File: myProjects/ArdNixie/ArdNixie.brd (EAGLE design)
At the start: 100 x 80 mm, 25 parts, among them IC1 74141, IC4 Anode Driver, IC5 SPARKRTC, X5 Seconds

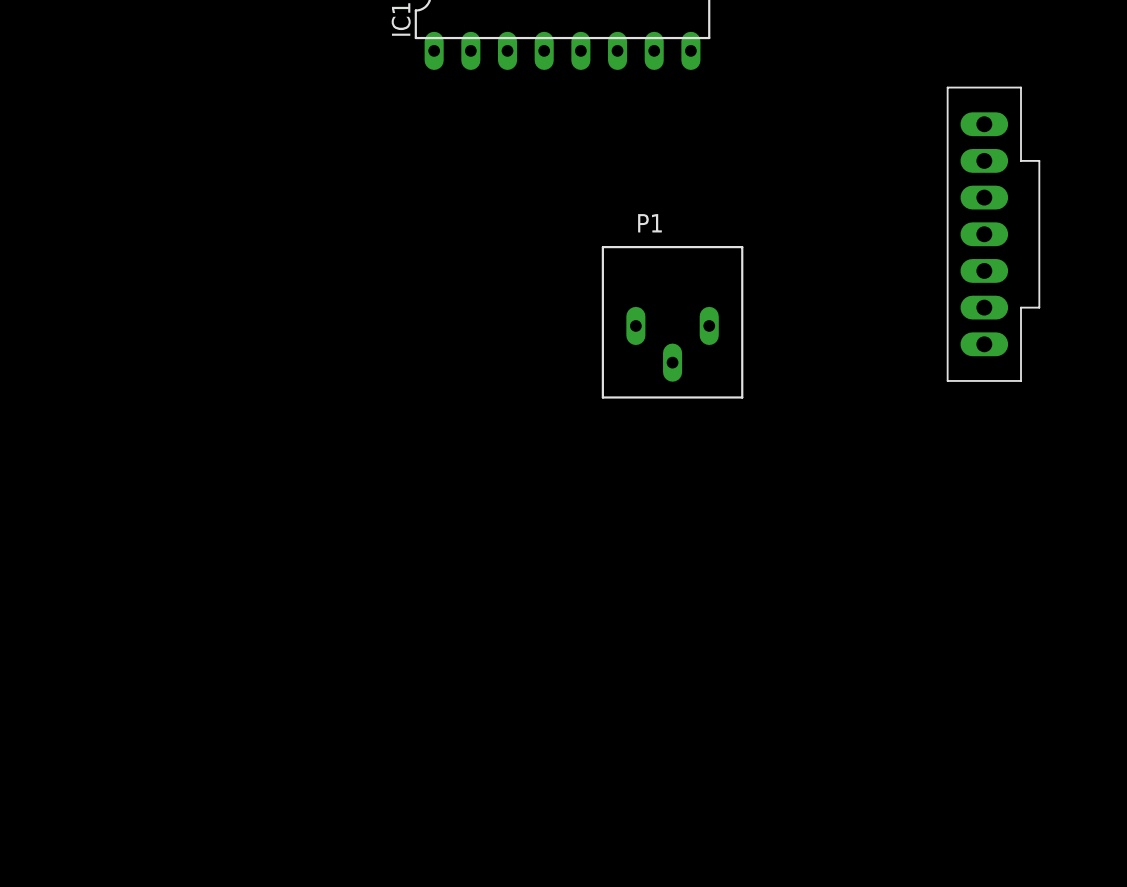
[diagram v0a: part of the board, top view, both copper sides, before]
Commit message: finished premil board layout for ardnixie
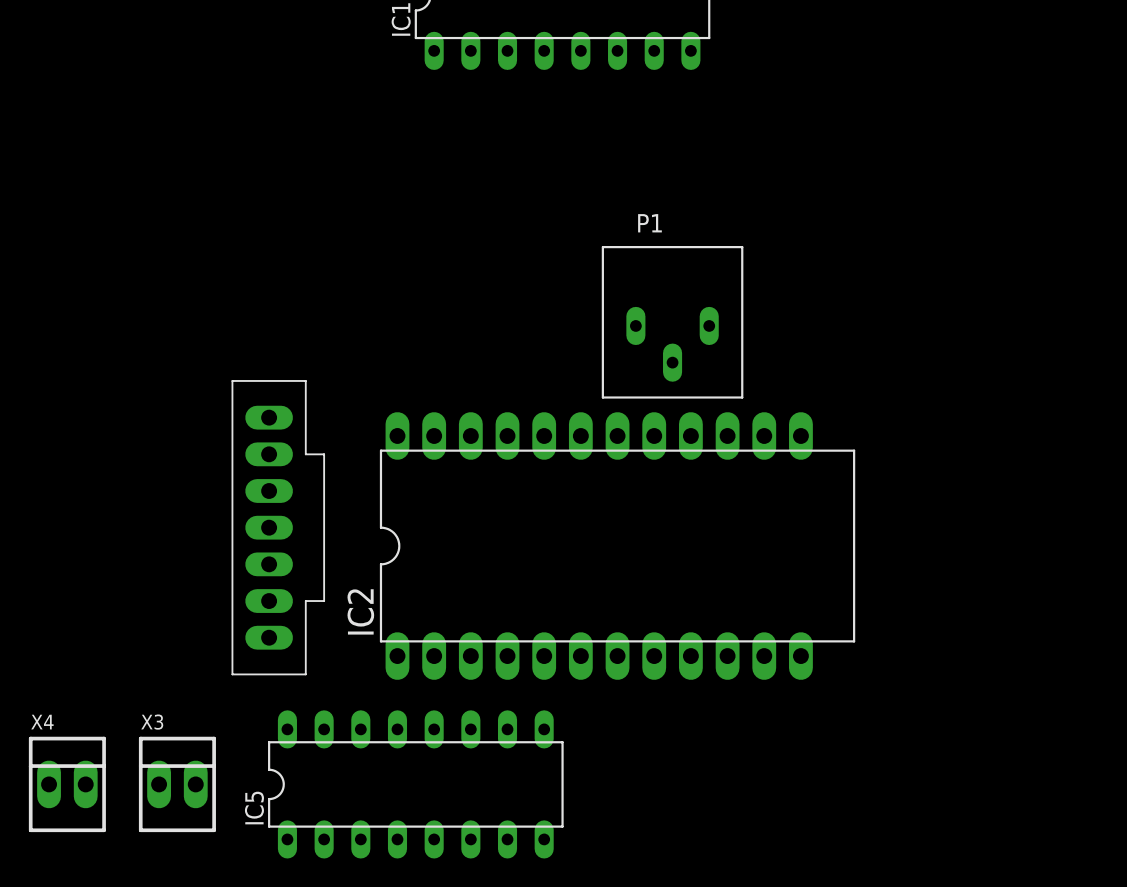
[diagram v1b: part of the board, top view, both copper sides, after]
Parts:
- added IC2: PRO-MINI, sibosop:DIL24-6-EXT
- added IC3: SPARKRTC, sibosop:SPARKRTC
- added X3: Hour Connector, sibosop-con-molex:22-23-2021
- added X4: Minute Connector, sibosop-con-molex:22-23-2021
- IC5: value SPARKRTC -> 74LS595N; device sibosop:SPARKRTC -> 74xx-us:DIL16
- X2: value (none) -> 12V
- moved IC5 54.8 mm to (-73.7, -26.7)
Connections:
- removed net +12V: X2.1
- new net N$1: IC5.15, R7.1
- new net N$17: IC1.7, IC5.6
- new net N$18: IC1.4, IC5.7
- new net N$19: IC2.24, X2.1
- new net N$2: IC5.1, R6.1
- new net N$20: IC2.11, IC3.SS
- new net N$22: IC2.16, IC3.CLK, IC5.11
- new net N$23: IC2.15, IC3.MISO
- new net N$27: IC2.14, IC3.MOSI, IC5.14
- new net N$28: IC2.5, IC3.SQW
- new net N$29: IC2.12, IC5.13
- new net N$3: IC5.2, R3.1
- new net N$30: IC2.13, IC5.12
- new net N$31: IC2.6, P1.A
- new net N$34: IC2.8, X4.1
- new net N$4: IC5.3, R2.1
- new net N$43: IC2.9, X3.1
- new net N$5: IC1.3, IC5.4
- new net N$6: IC1.6, IC5.5
- net VDD: now also IC2.21, IC3.VCC, IC5.10, IC5.16; no longer IC5.VCC
- net VSS: now also IC2.23, IC2.4, IC3.GND, IC5.8, X3.2, X4.2; no longer IC5.GND
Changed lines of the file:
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@@
 <element name="IC1" library="sibosop" package="DIP16" value="74141" x="-63.5" y="27.94"/>
 <element name="IC4" library="sibosop" package="DIP16" value="Anode Driver" x="-24.13" y="40.64"/>
-<element name="IC5" library="sibosop" package="SPARKRTC" value="SPARKRTC" x="-34.29" y="11.43"/>
 <element name="P1" library="sibosop" package="RJ6S" value="" x="-55.88" y="5.08"/>
 <element name="R10" library="rcl" package="0204V" value="33K" x="-25.4" y="80.01"/>
@@
 <element name="U$7" library="sibosop" package="HOLE-125" value="HOLE-125" x="-24.13" y="73.66"/>
 <element name="X1" library="sibosop-con-molex" package="22-23-2021" value="" x="-40.64" y="63.5"/>
-<element name="X2" library="sibosop-con-molex" package="22-23-2021" value="" x="-46.99" y="63.5"/>
+<element name="X2" library="sibosop-con-molex" package="22-23-2021" value="12V" x="-46.99" y="63.5"/>
 <element name="X5" library="sibosop-con-molex" package="22-23-2021" value="Seconds" x="-76.2" y="53.34"/>
+<element name="IC2" library="sibosop" package="DIL24-6-EXT" value="PRO-MINI" x="-62.23" y="-10.16"/>
+<element name="IC3" library="sibosop" package="SPARKRTC" value="SPARKRTC" x="-83.82" y="-8.89"/>
+<element name="IC5" library="74xx-us" package="DIL16" value="74LS595N" x="-73.66" y="-26.67"/>
+<element name="X3" library="sibosop-con-molex" package="22-23-2021" value="Hour Connector" x="-90.17" y="-26.67"/>
+<element name="X4" library="sibosop-con-molex" package="22-23-2021" value="Minute Connector" x="-97.79" y="-26.67"/>
 </elements>
 <signals>
-<signal name="VDD">
-<contactref element="C7" pad="2"/>
-<contactref element="IC1" pad="5"/>
-<contactref element="IC5" pad="VCC"/>
-<wire x1="-34.29" y1="6.35" x2="-62.23" y2="24.13" width="0" layer="19" extent="1-1"/>
-<wire x1="-44.45" y1="73.66" x2="-62.23" y2="24.13" width="0" layer="19" extent="1-1"/>
-</signal>
 <signal name="VSS">
 <contactref element="IC1" pad="12"/>
@@
 <contactref element="X1" pad="2"/>
 <contactref element="X5" pad="2"/>
-<contactref element="IC5" pad="GND"/>
+<contactref element="IC3" pad="GND"/>
+<contactref element="IC2" pad="23"/>
+<contactref element="IC2" pad="4"/>
+<contactref element="X3" pad="2"/>
+<contactref element="X4" pad="2"/>
+<contactref element="IC5" pad="8"/>
+<wire x1="-88.9" y1="-26.67" x2="-96.52" y2="-26.67" width="0" layer="19" extent="1-1"/>
+<wire x1="-83.82" y1="-16.51" x2="-88.9" y2="-26.67" width="0" layer="19" extent="1-1"/>
+<wire x1="-67.31" y1="-17.78" x2="-83.82" y2="-16.51" width="0" layer="19" extent="1-1"/>
+<wire x1="-64.77" y1="-30.48" x2="-67.31" y2="-17.78" width="0" layer="19" extent="1-1"/>
+<wire x1="-72.39" y1="-2.54" x2="-67.31" y2="-17.78" width="0" layer="19" extent="1-1"/>
+<wire x1="-62.23" y1="31.75" x2="-72.39" y2="-2.54" width="0" layer="19" extent="1-1"/>
 <wire x1="-74.93" y1="53.34" x2="-62.23" y2="31.75" width="0" layer="19" extent="1-1"/>
 <wire x1="-45.72" y1="63.5" x2="-74.93" y2="53.34" width="0" layer="19" extent="1-1"/>
@@
 <wire x1="-20.32" y1="36.83" x2="-25.4" y2="36.83" width="0" layer="19" extent="1-1"/>
 <wire x1="-15.24" y1="36.83" x2="-20.32" y2="36.83" width="0" layer="19" extent="1-1"/>
-<wire x1="-34.29" y1="3.81" x2="-30.48" y2="36.83" width="0" layer="19" extent="1-1"/>
 </signal>
 <signal name="N$7">
@@
 <wire x1="-50.8" y1="57.15" x2="-36.83" y2="80.01" width="0" layer="19" extent="1-1"/>
 </signal>
-<signal name="+12V">
-<contactref element="X2" pad="1"/>
-</signal>
 <signal name="N$61">
 <contactref element="IC4" pad="16"/>
@@
 <wire x1="-77.47" y1="53.34" x2="-58.42" y2="5.08" width="0" layer="19" extent="1-1"/>
 </signal>
+<signal name="N$1">
+<contactref element="IC5" pad="15"/>
+<contactref element="R7" pad="1"/>
+<wire x1="-16.51" y1="80.01" x2="-80.01" y2="-22.86" width="0" layer="19" extent="1-1"/>
+</signal>
+<signal name="N$2">
+<contactref element="IC5" pad="1"/>
+<contactref element="R6" pad="1"/>
+<wire x1="-77.47" y1="73.66" x2="-82.55" y2="-30.48" width="0" layer="19" extent="1-1"/>
+</signal>
+<signal name="N$3">
+<contactref element="IC5" pad="2"/>
+<contactref element="R3" pad="1"/>
+<wire x1="-62.23" y1="73.66" x2="-80.01" y2="-30.48" width="0" layer="19" extent="1-1"/>
+</signal>
+<signal name="N$4">
+<contactref element="IC5" pad="3"/>
+<contactref element="R2" pad="1"/>
+<wire x1="-57.15" y1="73.66" x2="-77.47" y2="-30.48" width="0" layer="19" extent="1-1"/>
+</signal>
+<signal name="N$5">
+<contactref element="IC5" pad="4"/>
+<contactref element="IC1" pad="3"/>
+<wire x1="-67.31" y1="24.13" x2="-74.93" y2="-30.48" width="0" layer="19" extent="1-1"/>
+</signal>
+<signal name="N$6">
+<contactref element="IC5" pad="5"/>
+<contactref element="IC1" pad="6"/>
+<wire x1="-59.69" y1="24.13" x2="-72.39" y2="-30.48" width="0" layer="19" extent="1-1"/>
+</signal>
+<signal name="N$17">
+<contactref element="IC5" pad="6"/>
+<contactref element="IC1" pad="7"/>
+<wire x1="-57.15" y1="24.13" x2="-69.85" y2="-30.48" width="0" layer="19" extent="1-1"/>
+</signal>
+<signal name="N$18">
+<contactref element="IC5" pad="7"/>
+<contactref element="IC1" pad="4"/>
+<wire x1="-64.77" y1="24.13" x2="-67.31" y2="-30.48" width="0" layer="19" extent="1-1"/>
+</signal>
+<signal name="N$19">
+<contactref element="IC2" pad="24"/>
+<contactref element="X2" pad="1"/>
+<wire x1="-48.26" y1="63.5" x2="-74.93" y2="-2.54" width="0" layer="19" extent="1-1"/>
+</signal>
+<signal name="VDD">
+<contactref element="IC2" pad="21"/>
+<contactref element="IC3" pad="VCC"/>
+<contactref element="IC5" pad="10"/>
+<contactref element="C7" pad="2"/>
+<contactref element="IC1" pad="5"/>
+<contactref element="IC5" pad="16"/>
+<wire x1="-83.82" y1="-13.97" x2="-82.55" y2="-22.86" width="0" layer="19" extent="1-1"/>
+<wire x1="-67.31" y1="-22.86" x2="-82.55" y2="-22.86" width="0" layer="19" extent="1-1"/>
+<wire x1="-67.31" y1="-2.54" x2="-83.82" y2="-13.97" width="0" layer="19" extent="1-1"/>
+<wire x1="-62.23" y1="24.13" x2="-67.31" y2="-2.54" width="0" layer="19" extent="1-1"/>
+<wire x1="-44.45" y1="73.66" x2="-62.23" y2="24.13" width="0" layer="19" extent="1-1"/>
+</signal>
+<signal name="N$20">
+<contactref element="IC3" pad="SS"/>
+<contactref element="IC2" pad="11"/>
+<wire x1="-49.53" y1="-17.78" x2="-83.82" y2="-1.27" width="0" layer="19" extent="1-1"/>
+</signal>
+<signal name="N$22">
+<contactref element="IC3" pad="CLK"/>
+<contactref element="IC2" pad="16"/>
+<contactref element="IC5" pad="11"/>
+<wire x1="-69.85" y1="-22.86" x2="-83.82" y2="-8.89" width="0" layer="19" extent="1-1"/>
+<wire x1="-54.61" y1="-2.54" x2="-69.85" y2="-22.86" width="0" layer="19" extent="1-1"/>
+</signal>
+<signal name="N$23">
+<contactref element="IC3" pad="MISO"/>
+<contactref element="IC2" pad="15"/>
+<wire x1="-52.07" y1="-2.54" x2="-83.82" y2="-6.35" width="0" layer="19" extent="1-1"/>
+</signal>
+<signal name="N$27">
+<contactref element="IC3" pad="MOSI"/>
+<contactref element="IC2" pad="14"/>
+<contactref element="IC5" pad="14"/>
+<wire x1="-83.82" y1="-3.81" x2="-77.47" y2="-22.86" width="0" layer="19" extent="1-1"/>
+<wire x1="-49.53" y1="-2.54" x2="-83.82" y2="-3.81" width="0" layer="19" extent="1-1"/>
+</signal>
+<signal name="N$28">
+<contactref element="IC3" pad="SQW"/>
+<contactref element="IC2" pad="5"/>
+<wire x1="-64.77" y1="-17.78" x2="-83.82" y2="-11.43" width="0" layer="19" extent="1-1"/>
+</signal>
+<signal name="N$29">
+<contactref element="IC2" pad="12"/>
+<contactref element="IC5" pad="13"/>
+<wire x1="-46.99" y1="-17.78" x2="-74.93" y2="-22.86" width="0" layer="19" extent="1-1"/>
+</signal>
+<signal name="N$30">
+<contactref element="IC2" pad="13"/>
+<contactref element="IC5" pad="12"/>
+<wire x1="-46.99" y1="-2.54" x2="-72.39" y2="-22.86" width="0" layer="19" extent="1-1"/>
+</signal>
+<signal name="N$31">
+<contactref element="IC2" pad="6"/>
+<contactref element="P1" pad="A"/>
+<wire x1="-53.34" y1="5.08" x2="-62.23" y2="-17.78" width="0" layer="19" extent="1-1"/>
+</signal>
+<signal name="N$34">
+<contactref element="X4" pad="1"/>
+<contactref element="IC2" pad="8"/>
+<wire x1="-57.15" y1="-17.78" x2="-99.06" y2="-26.67" width="0" layer="19" extent="1-1"/>
+</signal>
+<signal name="N$43">
+<contactref element="X3" pad="1"/>
+<contactref element="IC2" pad="9"/>
+<wire x1="-54.61" y1="-17.78" x2="-91.44" y2="-26.67" width="0" layer="19" extent="1-1"/>
+</signal>
 </signals>

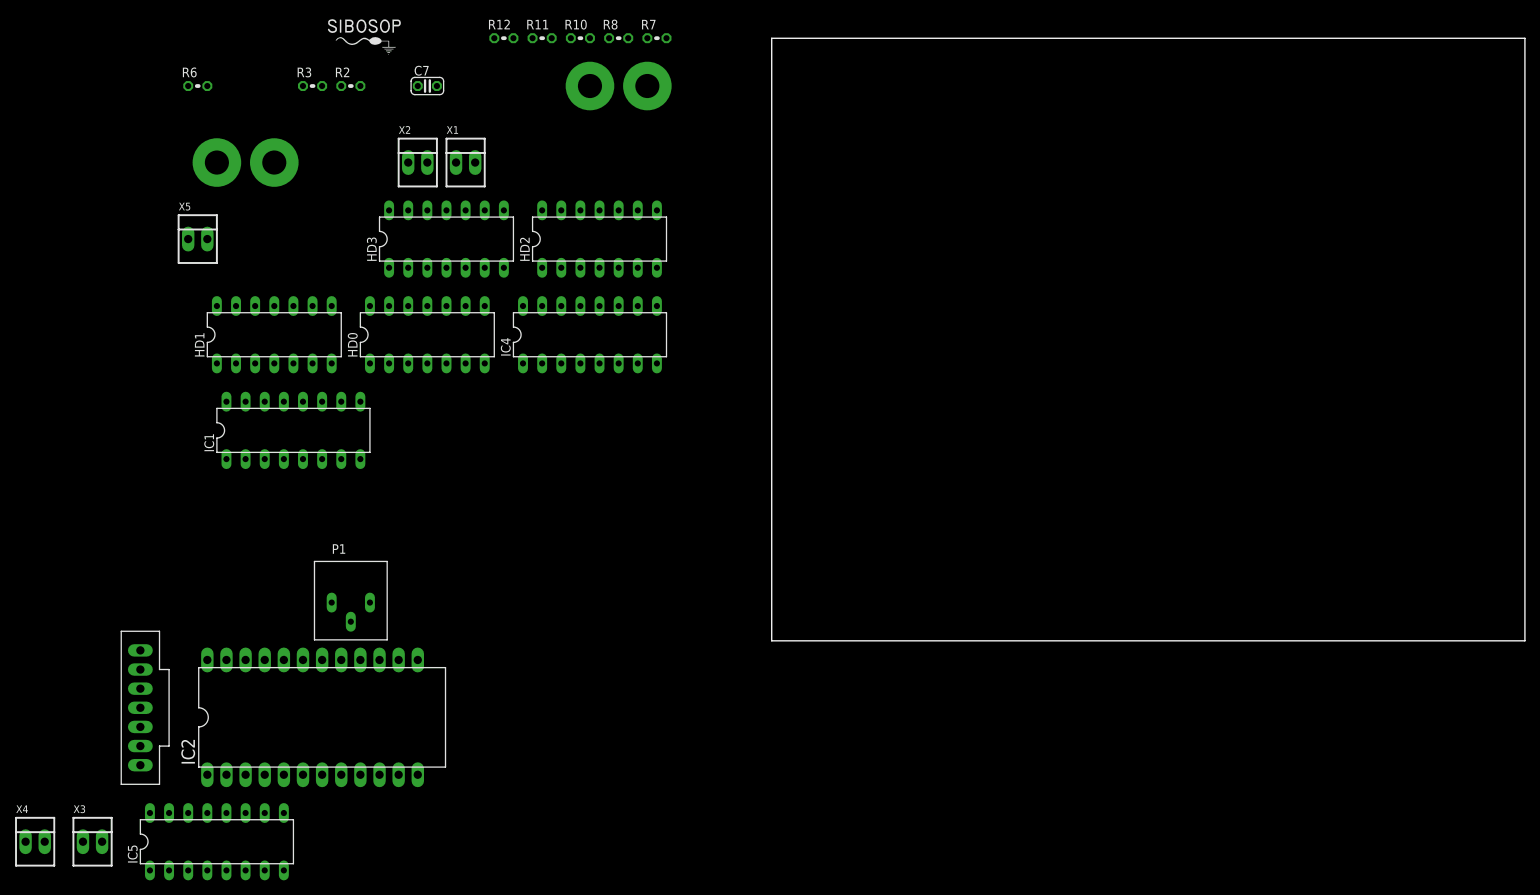
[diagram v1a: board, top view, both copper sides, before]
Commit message: finished first board design for ArdNixie
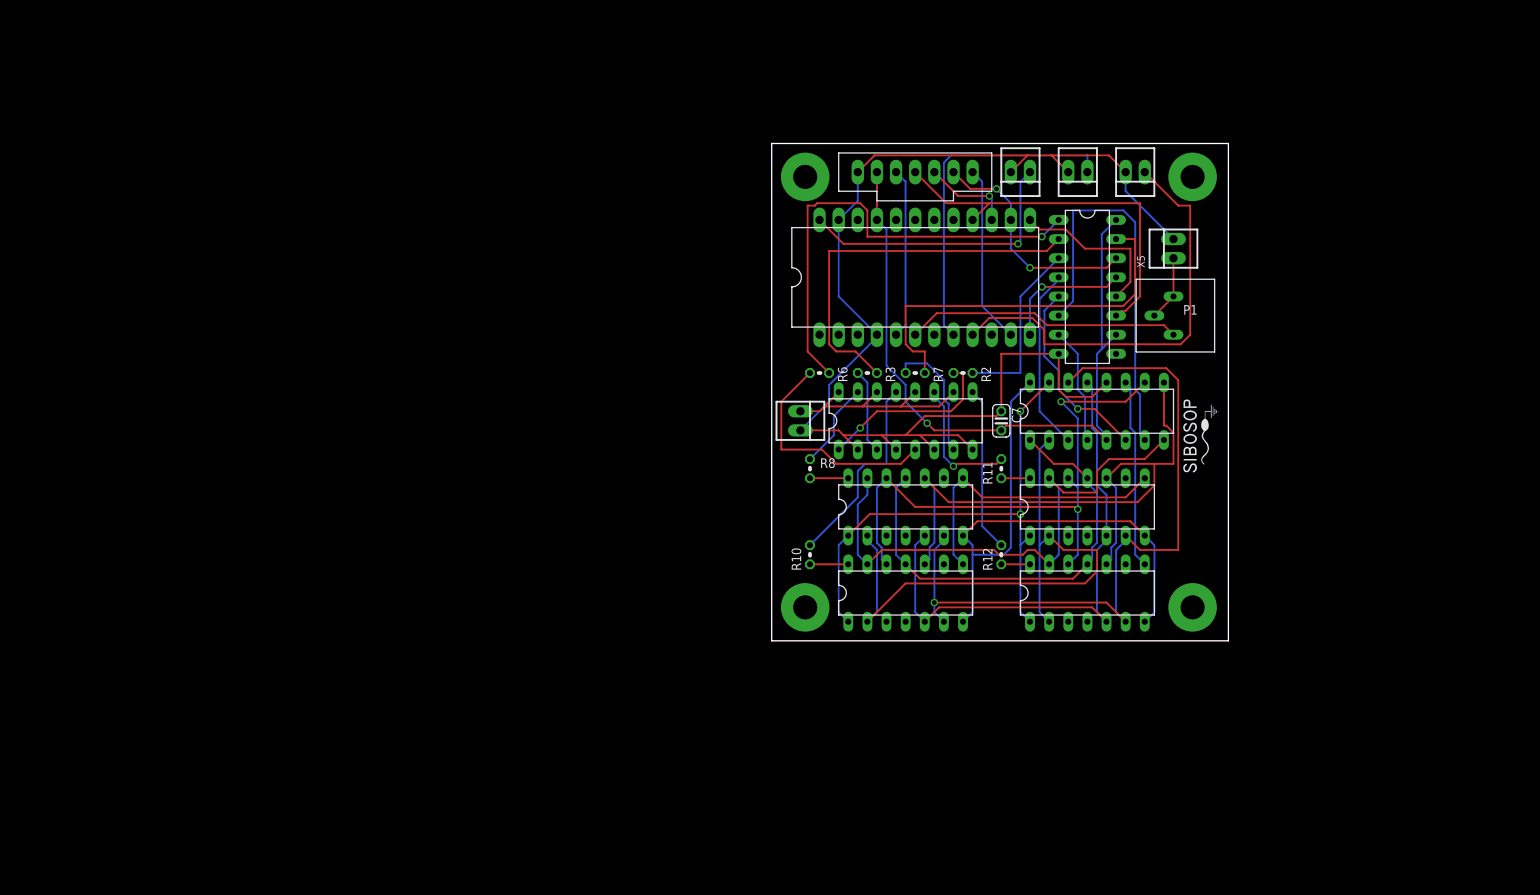
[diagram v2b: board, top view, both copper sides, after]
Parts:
- P1: value (none) -> s adj
- X1: value (none) -> HIV
- X3: value Hour Connector -> Hr
- X4: value Minute Connector -> Min
- moved X3 164.5 mm to (48.3, 62.2), turned to 180 degrees
- moved X4 164.5 mm to (40.6, 62.2), turned to 180 degrees
- moved U$2 142.4 mm to (55.9, 4.45)
- moved IC5 137.0 mm to (41.9, 47.0), turned to 270 degrees
- moved X5 129.5 mm to (53.3, 52.1), turned to 90 degrees
- moved IC3 125.1 mm to (19.1, 62.2), turned to 270 degrees
- moved U$3 123.2 mm to (55.9, 26.7), turned to 90 degrees
- moved P1 115.7 mm to (53.3, 43.2), turned to 270 degrees
- moved IC1 106.7 mm to (43.2, 30.5)
- moved IC2 100.1 mm to (19.1, 48.3)
- moved HD3 97.2 mm to (41.9, 6.35)
- moved R12 95.2 mm to (30.5, 11.4), turned to 90 degrees
- moved U$1 92.0 mm to (4.45, 4.45)
- moved R6 90.9 mm to (6.35, 35.6), turned to 180 degrees
- moved HD1 90.6 mm to (17.8, 6.35)
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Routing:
- net VSS: track 0.00 -> 170.4 mm
- net N$21: track 0.00 -> 97.8 mm, vias 0 -> 1
- net VDD: track 0.00 -> 94.8 mm, vias 0 -> 1
- net N$16: track 0.00 -> 82.7 mm
- net N$10: track 0.00 -> 81.7 mm
- net N$7: track 0.00 -> 79.1 mm
- net N$14: track 0.00 -> 76.6 mm, vias 0 -> 2
- net N$8: track 0.00 -> 72.2 mm, vias 0 -> 2
- net N$11: track 0.00 -> 72.0 mm
- net N$9: track 0.00 -> 71.8 mm
- net N$13: track 0.00 -> 65.7 mm
- net N$2: track 0.00 -> 61.7 mm, vias 0 -> 1
- net N$15: track 0.00 -> 60.4 mm
- net N$43: track 0.00 -> 57.9 mm
- net N$17: track 0.00 -> 53.1 mm
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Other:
- board size 100 x 80 mm -> 60.6 x 66 mm
- board text added: "2015-12-29"
- board text added: "Ard Nixie"
